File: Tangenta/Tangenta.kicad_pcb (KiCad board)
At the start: 4 copper layers, 243.8 x 243.8 mm, 83 parts, among them J1 39281243, J2 Conn_02x02_Top_Bottom, J3 10018784-10213TLF, J4 10018784-10213TLF, Q1 2N7002, Q2 2N7002, U1 TPS54331DR, U2 TPS54331DR, U3 TPS54331DR, U4 TPS54331DR, U5 74HC74D,653, U6 CD4060SA_TR, U7 74HC04D,653

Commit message: Current progress...
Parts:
- moved L1 266.4 mm to (98.5, 55.4), turned to -90 degrees
- moved D1 264.4 mm to (89.7, 58.4), turned to 180 degrees
- moved C10 256.8 mm to (88.1, 45.7), turned to 180 degrees
- moved C9 252.8 mm to (81.0, 68.1), turned to 90 degrees
- moved R13 248.1 mm to (93.7, 66.3)
- moved C6 243.8 mm to (75.9, 62.0), turned to 90 degrees
- moved R12 243.5 mm to (98.0, 65.5), turned to 90 degrees
- moved C7 242.4 mm to (91.2, 65.5), turned to -90 degrees
- moved R11 241.6 mm to (98.9, 68.1), turned to 180 degrees
- moved C8 238.0 mm to (96.3, 65.5), turned to -90 degrees
- moved C5 232.6 mm to (88.8, 50.5), turned to 180 degrees
- moved U1 227.7 mm to (86.1, 65.3), turned to -90 degrees
- moved C20 47.6 mm to (336.0, 168.2)
- moved U2 43.9 mm to (333.1, 72.7)
- moved U5 22.8 mm to (365.5, 108.5)

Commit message: Current progress...
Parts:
- moved C2 244.0 mm to (89.8, 62.0)
- moved L2 239.4 mm to (129.0, 54.9), turned to -90 degrees
- moved D2 237.2 mm to (120.1, 57.8), turned to 180 degrees
- moved C17 229.4 mm to (119.0, 45.8), turned to 180 degrees
- moved C12 223.9 mm to (111.5, 68.1), turned to 90 degrees
- moved C15 219.7 mm to (120.3, 62.0)
- moved R14 219.2 mm to (124.2, 66.3)
- moved R16 216.7 mm to (128.5, 65.5), turned to 90 degrees
- moved U2 216.7 mm to (116.6, 65.3), turned to -90 degrees
- moved C13 215.6 mm to (121.7, 65.5), turned to -90 degrees
- moved C11 215.4 mm to (110.0, 57.8)
- moved R15 214.5 mm to (129.3, 68.0), turned to 180 degrees
- moved L3 213.5 mm to (159.5, 54.9), turned to -90 degrees
- moved C16 212.7 mm to (119.6, 50.6), turned to 180 degrees
- moved C14 211.6 mm to (126.7, 65.5), turned to -90 degrees
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
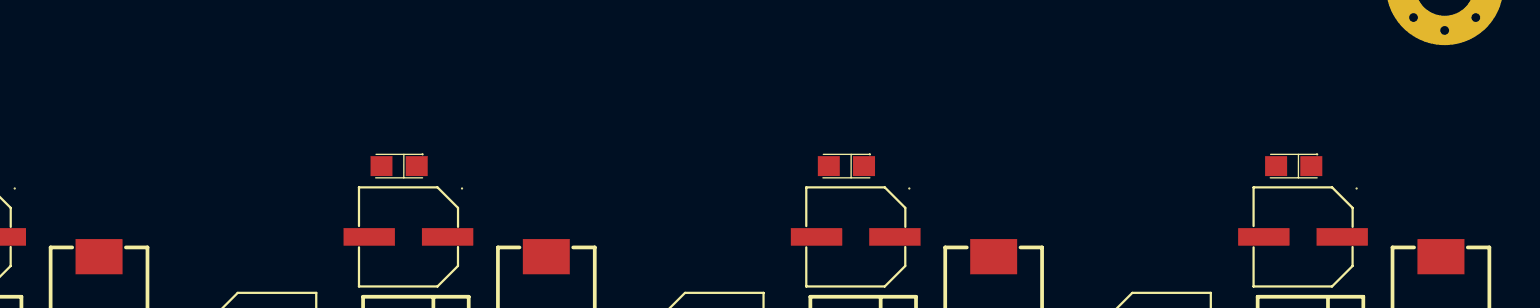
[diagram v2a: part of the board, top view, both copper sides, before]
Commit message: Power supply jumpers.
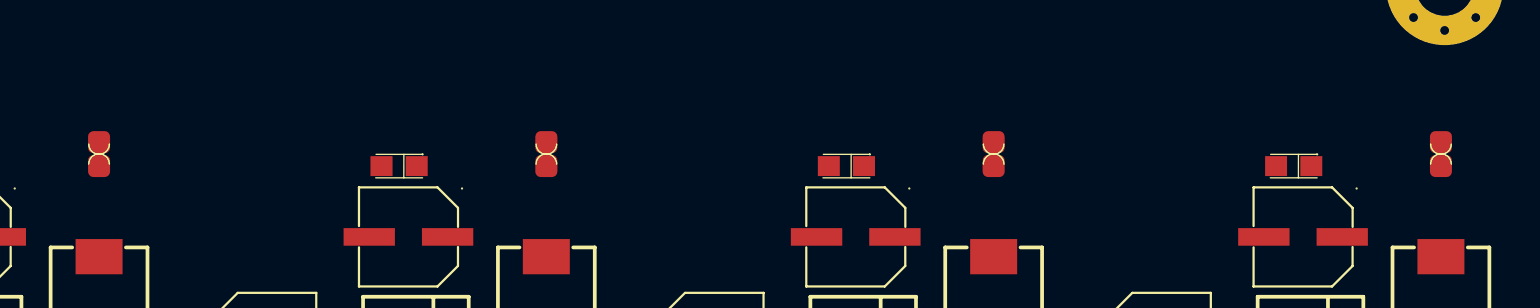
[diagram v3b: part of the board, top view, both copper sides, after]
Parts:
- added JP1: ~, CustomJumper:R_0805_2012Metric, F.Cu at (98.5, 45.0)
- added JP2: ~, CustomJumper:R_0805_2012Metric, F.Cu at (129.0, 45.0)
- added JP3: ~, CustomJumper:R_0805_2012Metric, F.Cu at (159.5, 45.0)
- added JP4: ~, CustomJumper:R_0805_2012Metric, F.Cu at (190.0, 45.0)

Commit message: Current progress...
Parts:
- H1: value MountingHole -> locked
- moved JP4 114.9 mm to (77.8, 70.2), turned to -90 degrees
- moved R21 114.7 mm to (77.5, 47.1), turned to 0 degrees
- moved L4 112.3 mm to (77.8, 60.3), turned to 90 degrees
- moved R22 112.3 mm to (78.3, 49.6), turned to -90 degrees
- moved C6 108.8 mm to (188.3, 57.3), turned to 180 degrees
- moved C28 108.7 mm to (80.1, 49.6), turned to 90 degrees
- moved C9 107.9 mm to (186.8, 47.0), turned to -90 degrees
- moved R20 104.0 mm to (82.7, 48.8), turned to 180 degrees
- moved C27 98.7 mm to (85.2, 49.6), turned to 90 degrees
- moved U1 96.9 mm to (181.7, 49.8), turned to 90 degrees
- moved C29 95.3 mm to (86.4, 53.1), turned to 180 degrees
- moved C31 95.0 mm to (87.9, 69.3), turned to 0 degrees
- moved C30 94.4 mm to (87.2, 64.5), turned to 0 degrees
- moved D4 94.4 mm to (86.7, 57.3), turned to 0 degrees
- moved C10 93.8 mm to (179.3, 69.3), turned to 0 degrees
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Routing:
- net Net-(U1-BOOT): track 0.00 -> 10.2 mm, vias 0 -> 2
- net Net-(U4-BOOT): track 0.00 -> 10.2 mm, vias 0 -> 2
- net Net-(U2-BOOT): track 0.00 -> 10.2 mm, vias 0 -> 2
- net Net-(U3-BOOT): track 0.00 -> 10.2 mm, vias 0 -> 2
- net GNDREF: vias 0 -> 32
- added copper zone on F.Cu, net GNDREF

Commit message: Routing...
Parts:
- added C32: 100nF, Capacitor_SMD:C_0603_1608Metric, F.Cu at (258.8, 123.3)
- added C33: 100nF, Capacitor_SMD:C_0603_1608Metric, F.Cu at (259.2, 111.6)
- added C34: 100nF, Capacitor_SMD:C_0603_1608Metric, F.Cu at (258.8, 133.9)
- moved R1 129.9 mm to (252.7, 93.5)
- moved R2 128.2 mm to (252.7, 101.5)
- moved Q2 128.0 mm to (259.3, 148.0)
- moved Q1 128.0 mm to (259.4, 140.2), turned to -90 degrees
- moved R3 127.9 mm to (252.0, 135.5), turned to -90 degrees
- moved C4 127.7 mm to (253.5, 95.9), turned to 90 degrees
- moved C3 126.1 mm to (253.5, 99.1), turned to -90 degrees
- moved R4 126.0 mm to (253.7, 135.5), turned to -90 degrees
- moved R9 126.0 mm to (258.4, 143.8), turned to 90 degrees
- moved C1 125.7 mm to (250.2, 135.5), turned to -90 degrees
- moved R10 125.2 mm to (258.6, 137.7)
- moved R8 124.2 mm to (260.4, 143.8), turned to 90 degrees
- moved R5 122.1 mm to (259.2, 113.3)
- moved R6 120.3 mm to (260.5, 152.3), turned to 180 degrees
- moved R7 119.8 mm to (260.5, 150.5), turned to 180 degrees
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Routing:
- net /ChassisButtons/VCC_LOGIC: track 0.00 -> 59.7 mm
- net /ChassisButtons/CONN_3: track 0.00 -> 49.8 mm
- net /ChassisButtons/PWR_BTN: track 0.00 -> 41.1 mm, vias 0 -> 1
- net /ChassisButtons/CONN_4: track 0.00 -> 37.1 mm
- net GNDREF: track 0.00 -> 19.7 mm, vias 32 -> 42
- net /ChassisButtons/ATX_GREEN_LINE: track 0.00 -> 14.8 mm
- net /ChassisButtons/CONN_2: track 0.00 -> 9.13 mm
- net /ChassisButtons/RST_BTN: track 0.00 -> 8.24 mm
- net /ChassisButtons/CONN_1: track 0.00 -> 7.98 mm
- net Net-(Q2-G): track 0.00 -> 3.71 mm
- net Net-(C1-Pad2): track 0.00 -> 3.58 mm
- net Net-(U6-CEXT): track 0.00 -> 3.16 mm
- net Net-(U6-RS): track 0.00 -> 3.12 mm
- net Net-(U6-REXT): track 0.00 -> 2.91 mm
- net Net-(U5-1D): track 0.00 -> 2.34 mm
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
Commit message: Current progress...
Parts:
- added J5: HY911130A, RJ45_MAGJACK:RJ45_MAGJACK_HY911130A, F.Cu at (48.8, 73.5)
- added J6: HY911130A, RJ45_MAGJACK:RJ45_MAGJACK_HY911130A, F.Cu at (48.8, 92.6)
- added J7: HY911130A, RJ45_MAGJACK:RJ45_MAGJACK_HY911130A, F.Cu at (48.8, 111.8)
- added J8: HY911130A, RJ45_MAGJACK:RJ45_MAGJACK_HY911130A, F.Cu at (48.8, 130.9)
- added J9: HC-SFP-01L, SFP_CAGE:TH_HC-SFP-01L, F.Cu at (58.4, 150.2)
- added S1: HC-SFP-20P, SFP_Connector:SFP_Connector, F.Cu at (69.6, 150.2)

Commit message: ...
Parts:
- added J10: 1-2199230-5, M2_Slot:M2_Slot, F.Cu at (74.7, 207.7)
- added J11: TYPEC-304-ACP16, USB_TYPEC:USB_TYPEC, F.Cu at (40.5, 32.8)
- added J12: 907-211A1019D10200, USB_2_CONNECTOR:USB_2_CONNECTOR, F.Cu at (44.8, 45.3)
- added J13: 906-861A2116D10210, USB_VERTICAL:USB_Vertical, F.Cu at (43.9, 56.5)
- added J14: RC01133, RJ45_SIMPLE:RJ45_SIMPLE, F.Cu at (41.6, 157.9)
- added J15: RC01133, RJ45_SIMPLE:RJ45_SIMPLE, F.Cu at (41.6, 177.3)
- added J16: TF-115K, MicroSD_Holder:MicroSD_Holder, F.Cu at (92.6, 36.9)
- added J17: 2309410-1, SODIMM_DDR4:SODIMM_DDR4, F.Cu at (153.8, 102.6)
- added J18: 1-2199230-5, M2_Slot:M2_Slot, F.Cu at (74.7, 253.4)
- added J19: HYC90-SIM06-180, SIM_Holder:SIM-SMD_HYC90-SIM06-180, F.Cu at (51.0, 256.3)
- J8: value HY911130A -> HDMI_19PIN_043; footprint RJ45_MAGJACK:RJ45_MAGJACK_HY911130A -> HDMI_CONNECTOR:HDMI_CONNECTOR
- moved J8 63.0 mm to (43.3, 68.1)
- moved J5 11.9 mm to (48.8, 85.3)
- moved J6 11.5 mm to (48.8, 104.1)
- moved J7 11.2 mm to (48.8, 122.9)
- moved J9 9.56 mm to (58.3, 140.6)
- moved S1 7.60 mm to (69.4, 142.6)
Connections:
- J8 pad 10: (no net) -> unconnected-(J8-TMDSClock+-Pad10)
- J8 pad 9: (no net) -> unconnected-(J8-TMDSData0--Pad9)

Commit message: Current progress with the USB schematics...
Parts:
- moved S1 1.94 mm to (69.6, 140.7)
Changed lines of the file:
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@@
   )
   (footprint "SFP_Connector:SFP_Connector" (layer "F.Cu")
-    (at 69.427051 142.649152 -90)
+    (at 69.59 140.718 -90)
     (descr "CONN-SMD_20P-P0.80_HCTL_HC-SFP-20P footprint")
     (tags "CONN-SMD_20P-P0.80_HCTL_HC-SFP-20P footprint")
